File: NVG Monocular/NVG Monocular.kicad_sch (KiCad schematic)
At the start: 26 parts, among them J1 USB4105-GF-A, J2 breakout to header pin, J3 I2C Breakout, J4 breakout to batt, U1 MP2696AGQ-0000-P

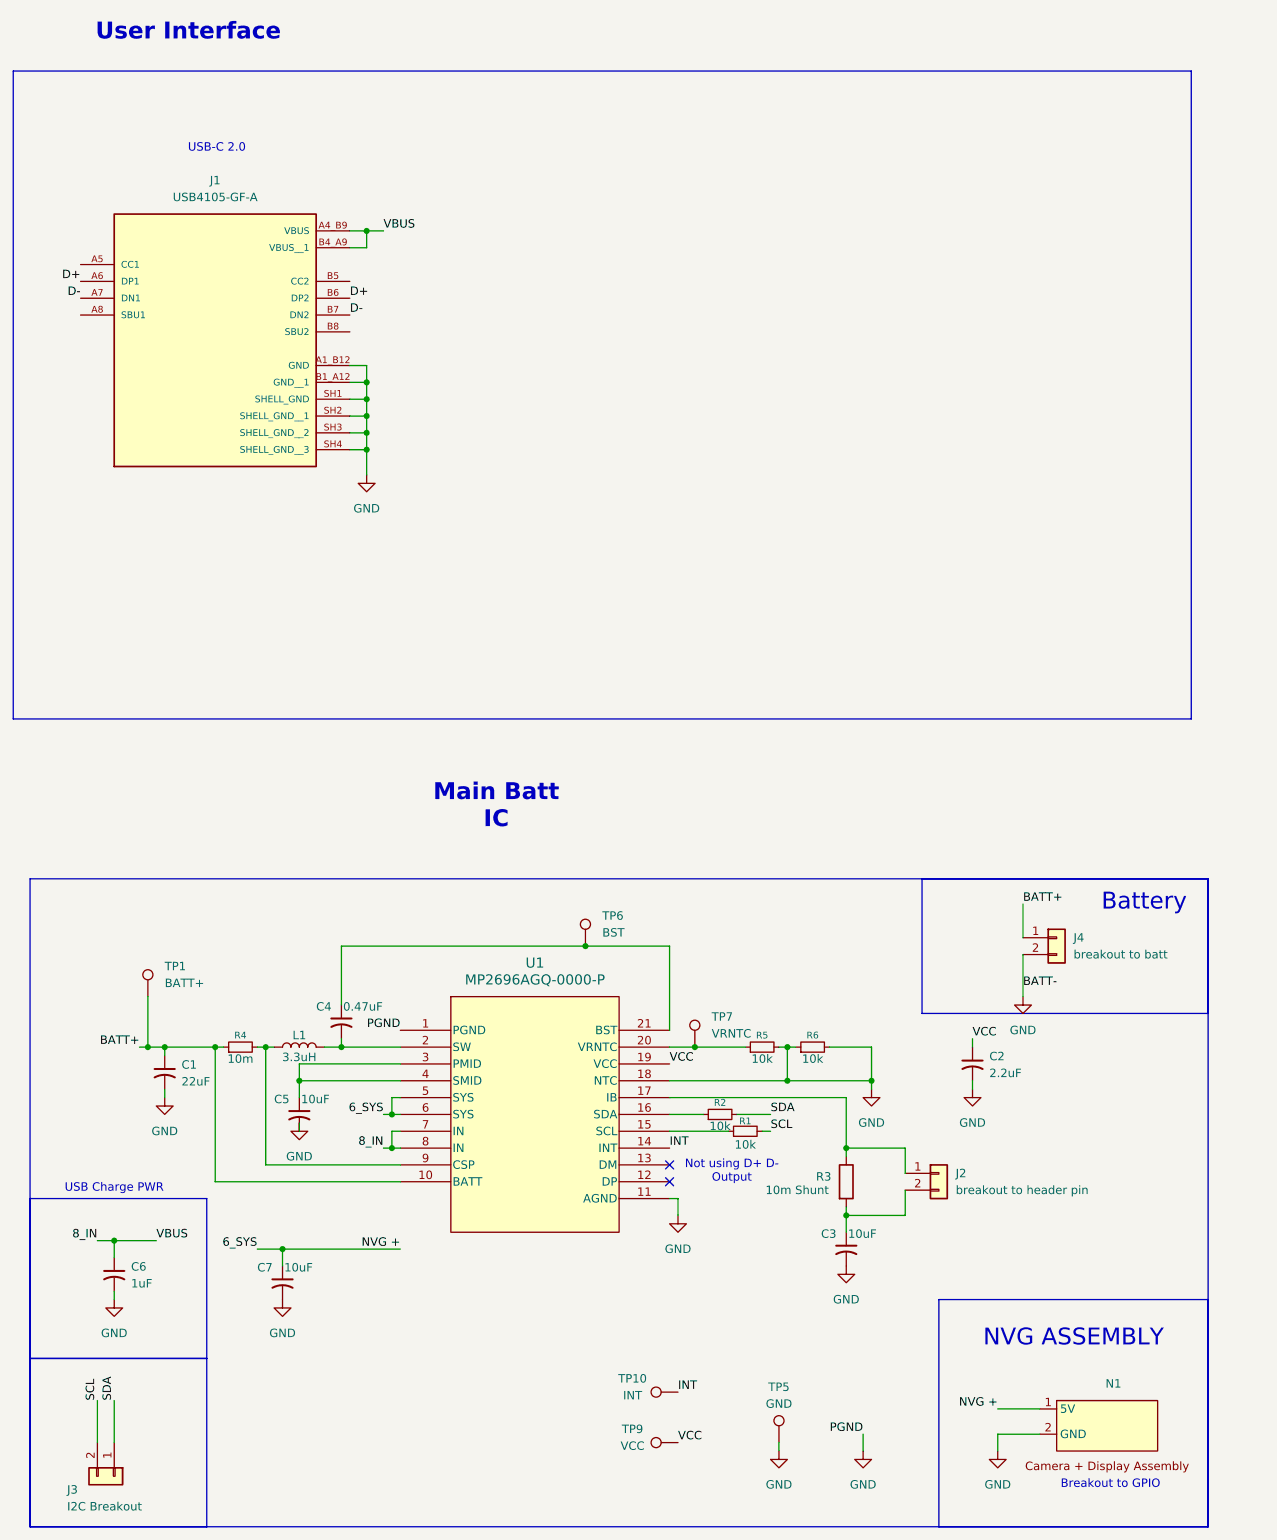
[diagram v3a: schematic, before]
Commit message: V1 breakout completed and ordered
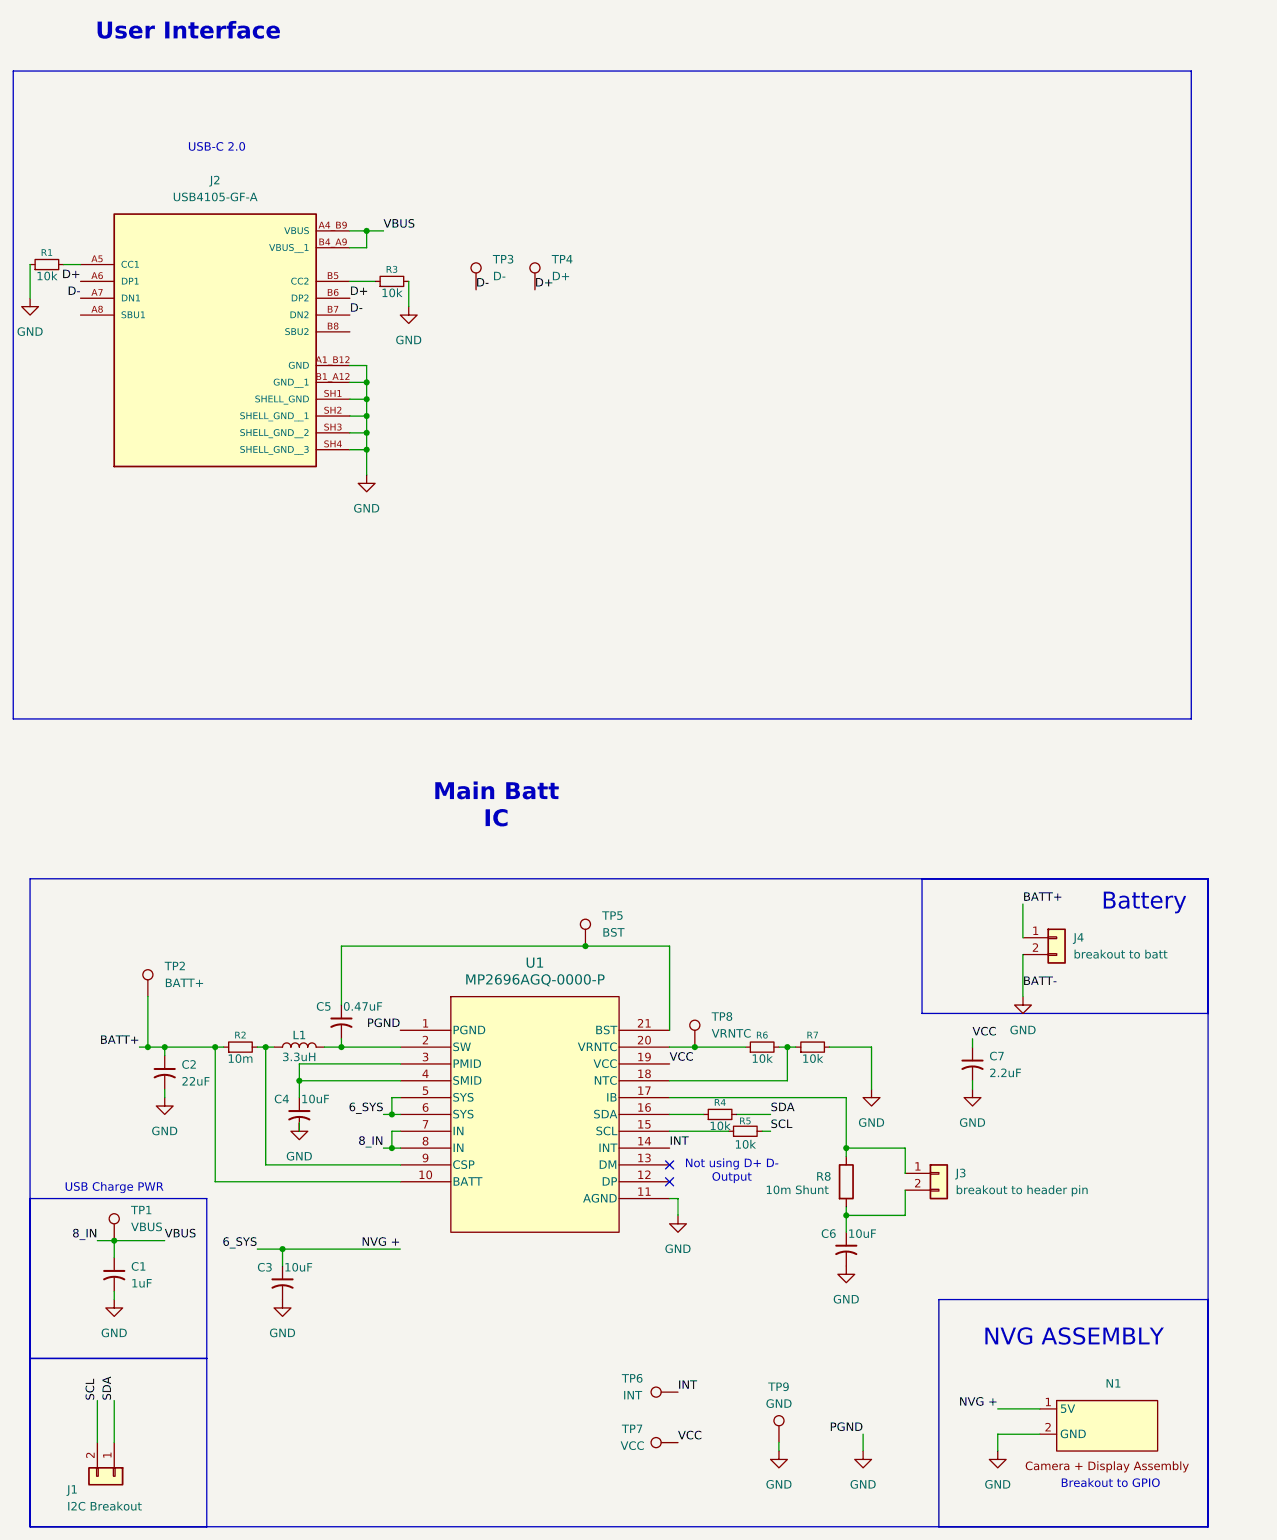
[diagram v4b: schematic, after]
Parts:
- added R1, R3: 10k, Resistor_SMD:R_0603_1608Metric, symbol Device:R_Small
- added TP1: VBUS, TestPoint:TestPoint_Pad_D1.5mm, symbol Connector:TestPoint
- added TP3: D-, TestPoint:TestPoint_Pad_D1.5mm, symbol Connector:TestPoint
- added TP4: D+, TestPoint:TestPoint_Pad_D1.5mm, symbol Connector:TestPoint
- renumbered C6 to C1, C1 to C2, C7 to C3, C5 to C4, C4 to C5, C3 to C6, C2 to C7, J3 to J1, J1 to J2, J2 to J3, R4 to R2, R2 to R4, R1 to R5, R5 to R6, R6 to R7, R3 to R8, TP1 to TP2, TP6 to TP5, TP10 to TP6, TP9 to TP7, TP7 to TP8, TP5 to TP9
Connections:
- net 8_IN: now also TP1.1
- net D+: now also TP4.1
- net D-: now also TP3.1
- net GND: now also R1.1, R3.2; no longer R6.2, R7.1, U1.18 (NTC)
- net at J2.A5 (CC1): now also R1.2
- net at J2.B5 (CC2): now also R3.1
- new net: R6.2, R7.1, U1.18 (NTC)
